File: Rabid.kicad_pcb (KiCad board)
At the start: 2 copper layers, 342.9 x 121.9 mm, 215 parts, among them J1 USB Header, SW1 Key, SW10 Key, SW100 Key, SW101 Key, SW102 Key, SW11 Key, SW12 Key, SW13 Key, SW14 Key, SW15 Key, SW16 Key, SW17 Key, SW18 Key, SW19 Key, SW2 Key, SW20 Key, SW21 Key, SW22 Key, SW23 Key, SW24 Key, SW25 Key, SW26 Key, SW27 Key, SW28 Key, SW29 Key, SW3 Key, SW30 Key, SW31 Key, SW32 Key, SW33 Key, SW34 Key, SW35 Key, SW36 Key, SW37 Key, SW38 Key, SW39 Key, SW4 Key, SW40 Key, SW41 Key, SW42 Key, SW43 Key, SW44 Key, SW45 Key, SW46 Key, SW47 Key, SW48 Key, SW49 Key, SW5 Key, SW50 Key, SW51 Key, SW52 Key, SW53 Key, SW54 Key, SW55 Key, SW56 Key, SW57 Key, SW58 Key, SW59 Key, SW6 Key, SW60 Key, SW61 Key, SW62 Key, SW63 Key, SW64 Key, SW65 Key, SW66 Key, SW67 Key, SW68 Key, SW69 Key, SW7 Key, SW70 Key, SW71 Key, SW72 Key, SW73 Key, SW74 Key, SW75 Key, SW76 Key, SW77 Key, SW78 Key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

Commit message: Everything in its approximate location.
TODO:
 - Still needs comparison to a real PCB to get measurements more accurate.
 - Needs mounting holes.
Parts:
- removed D100, D101, D24, D30, D36, D48, D54, D60, D7, D77, D82, D83, D88, D89, D94: 1N4148, Diode_THT:D_DO-35_SOD27_P7.62mm_Horizontal
- removed SW100, SW101, SW24, SW30, SW36, SW48, SW54, SW60, SW7, SW77, SW82, SW83, SW88, SW89, SW94: Key, Button_Switch_Keyboard:SW_Cherry_MX_1.00u_PCB
- SW12, SW18, SW6, SW66, SW72, SW78, SW84: footprint Button_Switch_Keyboard:SW_Cherry_MX_1.00u_PCB -> Button_Switch_Keyboard:SW_Cherry_MX_1.25u_PCB
- SW3, SW81: footprint Button_Switch_Keyboard:SW_Cherry_MX_1.00u_PCB -> Button_Switch_Keyboard:SW_Cherry_MX_1.50u_PCB
- SW4: footprint Button_Switch_Keyboard:SW_Cherry_MX_1.00u_PCB -> Button_Switch_Keyboard:SW_Cherry_MX_1.75u_PCB
- SW42: footprint Button_Switch_Keyboard:SW_Cherry_MX_1.00u_PCB -> Button_Switch_Keyboard:SW_Cherry_MX_6.25u_PCB
- SW5, SW76: footprint Button_Switch_Keyboard:SW_Cherry_MX_1.00u_PCB -> Button_Switch_Keyboard:SW_Cherry_MX_2.25u_PCB
- SW71: footprint Button_Switch_Keyboard:SW_Cherry_MX_1.00u_PCB -> Button_Switch_Keyboard:SW_Cherry_MX_2.75u_PCB
- SW80: footprint Button_Switch_Keyboard:SW_Cherry_MX_1.00u_PCB -> Button_Switch_Keyboard:SW_Cherry_MX_2.00u_PCB
- moved R2 420.4 mm to (335.5, 99.8)
- moved D91 413.8 mm to (348.0, 90.8), turned to 90 degrees
- moved D104 395.8 mm to (346.7, 99.6)
- moved D55 386.2 mm to (219.1, 90.8), turned to 90 degrees
- moved D99 384.1 mm to (367.7, 137.8), turned to 90 degrees
- moved D62 381.6 mm to (229.2, 118.7), turned to 90 degrees
- moved D87 366.9 mm to (328.9, 137.8), turned to 90 degrees
- moved D43 365.2 mm to (181.0, 90.8), turned to 90 degrees
- moved D2 359.4 mm to (51.3, 103.4), turned to 180 degrees
- moved R3 359.3 mm to (335.5, 103.4)
- moved D106 352.6 mm to (365.8, 99.8)
- moved D81 350.9 mm to (298.4, 137.8), turned to 90 degrees
- moved D1 347.3 mm to (57.4, 90.7), turned to 90 degrees
- moved D20 346.1 mm to (95.2, 118.7), turned to 90 degrees
- moved D49 346.0 mm to (200.0, 90.8), turned to 90 degrees
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
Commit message: Name the keys on F.Fab layer.
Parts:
- SW1: value Key -> Esc
- SW10: value Key -> A
- SW102: value Key -> →
- SW11: value Key -> Z
- SW12: value Key -> LMeta
- SW13: value Key -> F1
- SW14: value Key -> 2
- SW15: value Key -> W
- SW16: value Key -> S
- SW17: value Key -> X
- SW18: value Key -> LAlt
- SW19: value Key -> F2
- SW2: value Key -> ~
- SW20: value Key -> 3
- SW21: value Key -> E
- SW22: value Key -> D
- SW23: value Key -> C
- SW25: value Key -> F3
- SW26: value Key -> 4
- SW27: value Key -> R
- SW28: value Key -> F
- SW29: value Key -> V
- SW3: value Key -> Tab
- SW31: value Key -> F4
- SW32: value Key -> 5
- SW33: value Key -> T
- SW34: value Key -> G
- SW35: value Key -> B
- SW37: value Key -> F5
- SW38: value Key -> 6
- SW39: value Key -> Y
- SW4: value Key -> CapsLk
- SW40: value Key -> H
- SW41: value Key -> N
- SW42: value Key -> Space
- SW43: value Key -> F6
- SW44: value Key -> 7
- SW45: value Key -> U
- SW46: value Key -> J
- SW47: value Key -> M
- SW49: value Key -> F7
- SW5: value Key -> LShift
- SW50: value Key -> 8
- SW51: value Key -> I
- SW52: value Key -> K
- SW53: value Key -> ,
- SW55: value Key -> F8
- SW56: value Key -> 9
- SW57: value Key -> O
- SW58: value Key -> L
- SW59: value Key -> .
- SW6: value Key -> LCtrl
- SW61: value Key -> F9
- SW62: value Key -> 0
- SW63: value Key -> P
- SW64: value Key -> ;
- SW65: value Key -> /
- SW66: value Key -> AltGr
- SW67: value Key -> F10
- SW68: value Key -> -
- SW69: value Key -> [
- SW70: value Key -> "
- SW71: value Key -> RShift
- SW72: value Key -> RMeta
- SW73: value Key -> F11
- SW74: value Key -> =
- SW75: value Key -> ]
- SW76: value Key -> ↲
- SW78: value Key -> Fn
- SW79: value Key -> F12
- SW8: value Key -> 1
- SW80: value Key -> BkSpc
- SW81: value Key -> \
- SW84: value Key -> RCtrl
- SW85: value Key -> PrtSc
- SW86: value Key -> Ins
- SW87: value Key -> Del
- SW9: value Key -> Q
- SW90: value Key -> ←
- SW91: value Key -> ScrLk
- SW92: value Key -> Home
- SW93: value Key -> End
- SW95: value Key -> ↑
- SW96: value Key -> ↓
- SW97: value Key -> Pause
- SW98: value Key -> PgUp
- SW99: value Key -> PgDn

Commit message: Made measurements more precise.
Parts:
- J1: moved to B.Cu
- moved J1 57.4 mm to (295.7, 96.5), turned to 90 degrees
- moved SW1 0.25 mm to (50.2, 80.9)
- moved D105 0.13 mm to (356.2, 90.8)
- moved D107 0.13 mm to (255.9, 90.8)
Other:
- board size 342.9 x 121.9 mm -> 344.6 x 122 mm
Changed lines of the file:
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@@
       (effects (font (size 0.9 0.9) (thickness 0.12)))
     )
-    (fp_text user "0" (at -4.0372 -11.2 unlocked) (layer "F.SilkS")
+    (fp_text user "0" (at -11.303 -11.176 unlocked) (layer "F.SilkS")
       (effects (font (size 0.9 0.9) (thickness 0.12)))
     )
@@
     )
   )
-  (footprint "Connector_JST:JST_PH_S5B-PH-SM4-TB_1x05-1MP_P2.00mm_Horizontal" (layer "F.Cu")
-    (at 238.252 98.044 -90)
-    (descr "JST PH series connector, S5B-PH-SM4-TB (http://www.jst-mfg.com/product/pdf/eng/ePH.pdf), generated with kicad-footprint-generator")
-    (tags "connector JST PH top entry")
-    (property "Sheetfile" "Rabid.kicad_sch")
-    (property "Sheetname" "")
-    (attr smd)
-    (fp_text reference "J1" (at 0 -5.8 90) (layer "F.SilkS")
-      (effects (font (size 1 1) (thickness 0.15)))
-    )
-    (fp_text value "USB Header" (at 0 5.8 90) (layer "F.Fab")
-      (effects (font (size 1 1) (thickness 0.15)))
-    )
-    (fp_text user "${REFERENCE}" (at 0 1.5 90) (layer "F.Fab")
-      (effects (font (size 1 1) (thickness 0.15)))
-    )
-    (fp_line (start -5.34 4.51) (end 5.34 4.51) (layer "F.SilkS") (width 0.12))
-    (fp_line (start -6.04 -3.31) (end -6.04 -1.71) (layer "F.SilkS") (width 0.12))
-    (fp_line (start 7.06 0.94) (end 7.06 -3.31) (layer "F.SilkS") (width 0.12))
-    (fp_line (start 6.04 -3.31) (end 6.04 -1.71) (layer "F.SilkS") (width 0.12))
-    (fp_line (start -4.76 -1.71) (end -4.76 -4.6) (layer "F.SilkS") (width 0.12))
-    (fp_line (start -7.06 -3.31) (end -6.04 -3.31) (layer "F.SilkS") (width 0.12))
-    (fp_line (start 6.04 -1.71) (end 4.76 -1.71) (layer "F.SilkS") (width 0.12))
-    (fp_line (start 7.06 -3.31) (end 6.04 -3.31) (layer "F.SilkS") (width 0.12))
-    (fp_line (start -7.06 0.94) (end -7.06 -3.31) (layer "F.SilkS") (width 0.12))
-    (fp_line (start -6.04 -1.71) (end -4.76 -1.71) (layer "F.SilkS") (width 0.12))
-    (fp_line (start 7.6 5.1) (end 7.6 -5.1) (layer "F.CrtYd") (width 0.05))
-    (fp_line (start -7.6 5.1) (end 7.6 5.1) (layer "F.CrtYd") (width 0.05))
-    (fp_line (start -7.6 -5.1) (end -7.6 5.1) (layer "F.CrtYd") (width 0.05))
-    (fp_line (start 7.6 -5.1) (end -7.6 -5.1) (layer "F.CrtYd") (width 0.05))
-    (fp_line (start -6.95 -3.2) (end -6.15 -3.2) (layer "F.Fab") (width 0.1))
-    (fp_line (start 6.95 -3.2) (end 6.95 4.4) (layer "F.Fab") (width 0.1))
-    (fp_line (start -6.95 4.4) (end 6.95 4.4) (layer "F.Fab") (width 0.1))
-    (fp_line (start -4 -0.892893) (end -3.5 -1.6) (layer "F.Fab") (width 0.1))
-    (fp_line (start 6.15 -3.2) (end 6.95 -3.2) (layer "F.Fab") (width 0.1))
-    (fp_line (start -6.15 -3.2) (end -6.15 -1.6) (layer "F.Fab") (width 0.1))
-    (fp_line (start 6.15 -1.6) (end 6.15 -3.2) (layer "F.Fab") (width 0.1))
-    (fp_line (start -6.95 -3.2) (end -6.95 4.4) (layer "F.Fab") (width 0.1))
-    (fp_line (start -4.5 -1.6) (end -4 -0.892893) (layer "F.Fab") (width 0.1))
-    (fp_line (start -6.15 -1.6) (end 6.15 -1.6) (layer "F.Fab") (width 0.1))
-    (pad "1" smd roundrect (at -4 -2.85 270) (size 1 3.5) (layers "F.Cu" "F.Paste" "F.Mask") (roundrect_rratio 0.25)
-      (net 107 "Net-(J1-Pad1)") (pinfunction "Pin_1") (pintype "passive"))
-    (pad "2" smd roundrect (at -2 -2.85 270) (size 1 3.5) (layers "F.Cu" "F.Paste" "F.Mask") (roundrect_rratio 0.25)
-      (net 108 "Net-(J1-Pad2)") (pinfunction "Pin_2") (pintype "passive"))
-    (pad "3" smd roundrect (at 0 -2.85 270) (size 1 3.5) (layers "F.Cu" "F.Paste" "F.Mask") (roundrect_rratio 0.25)
-      (net 109 "Net-(J1-Pad3)") (pinfunction "Pin_3") (pintype "passive"))
-    (pad "4" smd roundrect (at 2 -2.85 270) (size 1 3.5) (layers "F.Cu" "F.Paste" "F.Mask") (roundrect_rratio 0.25)
-      (net 33 "GND") (pinfunction "Pin_4") (pintype "passive"))
-    (pad "5" smd roundrect (at 4 -2.85 270) (size 1 3.5) (layers "F.Cu" "F.Paste" "F.Mask") (roundrect_rratio 0.25)
-      (net 110 "unconnected-(J1-Pad5)") (pinfunction "Pin_5") (pintype "passive"))
-    (pad "MP" smd roundrect (at 6.35 2.9 270) (size 1.5 3.4) (layers "F.Cu" "F.Paste" "F.Mask") (roundrect_rratio 0.166667))
-    (pad "MP" smd roundrect (at -6.35 2.9 270) (size 1.5 3.4) (layers "F.Cu" "F.Paste" "F.Mask") (roundrect_rratio 0.166667))
-    (model "${KICAD6_3DMODEL_DIR}/Connector_JST.3dshapes/JST_PH_S5B-PH-SM4-TB_1x05-1MP_P2.00mm_Horizontal.wrl"
-      (offset (xyz 0 0 0))
-      (scale (xyz 1 1 1))
-      (rotate (xyz 0 0 0))
-    )
-  )
   (footprint "Button_Switch_Keyboard:SW_Cherry_MX_1.00u_PCB" (layer "F.Cu")
     (at 169.2402 165.7858)
@@
   )
   (footprint "Button_Switch_Keyboard:SW_Cherry_MX_1.00u_PCB" (layer "F.Cu")
-    (at 50.165 80.645)
+    (at 50.165 80.899)
     (descr "Cherry MX keyswitch, 1.00u, PCB mount, http://cherryamericas.com/wp-content/uploads/2014/12/mx_cat.pdf")
     (tags "Cherry MX keyswitch 1.00u PCB")
@@
   )
   (footprint "LED_THT:LED_D3.0mm" (layer "F.Cu")
-    (at 356.23 90.932)
+    (at 356.23 90.805)
     (descr "LED, diameter 3.0mm, 2 pins")
     (tags "LED diameter 3.0mm 2 pins")
@@
   )
   (footprint "LED_THT:LED_D3.0mm" (layer "F.Cu")
-    (at 255.9 90.932)
+    (at 255.9 90.805)
     (descr "LED, diameter 3.0mm, 2 pins")
     (tags "LED diameter 3.0mm 2 pins")
@@
     )
   )
-  (gr_rect (start 40.386 76.2) (end 383.286 198.12) (layer "Edge.Cuts") (width 0.1) (fill none))
+  (footprint "Connector_JST:JST_PH_S5B-PH-SM4-TB_1x05-1MP_P2.00mm_Horizontal" (layer "B.Cu")
+    (at 295.656 96.52 90)
+    (descr "JST PH series connector, S5B-PH-SM4-TB (http://www.jst-mfg.com/product/pdf/eng/ePH.pdf), generated with kicad-footprint-generator")
+    (tags "connector JST PH top entry")
+    (property "Sheetfile" "Rabid.kicad_sch")
+    (property "Sheetname" "")
+    (attr smd)
+    (fp_text reference "J1" (at 0 5.8 90) (layer "B.SilkS")
+      (effects (font (size 1 1) (thickness 0.15)) (justify mirror))
+    )
+    (fp_text value "USB Header" (at 0 -5.8 90) (layer "B.Fab")
+      (effects (font (size 1 1) (thickness 0.15)) (justify mirror))
+    )
+    (fp_text user "${REFERENCE}" (at 0 -1.5 90) (layer "B.Fab")
+      (effects (font (size 1 1) (thickness 0.15)) (justify mirror))
+    )
+    (fp_line (start -5.34 -4.51) (end 5.34 -4.51) (layer "B.SilkS") (width 0.12))
+    (fp_line (start -6.04 3.31) (end -6.04 1.71) (layer "B.SilkS") (width 0.12))
+    (fp_line (start 7.06 -0.94) (end 7.06 3.31) (layer "B.SilkS") (width 0.12))
+    (fp_line (start 6.04 3.31) (end 6.04 1.71) (layer "B.SilkS") (width 0.12))
+    (fp_line (start -4.76 1.71) (end -4.76 4.6) (layer "B.SilkS") (width 0.12))
+    (fp_line (start -7.06 3.31) (end -6.04 3.31) (layer "B.SilkS") (width 0.12))
+    (fp_line (start 6.04 1.71) (end 4.76 1.71) (layer "B.SilkS") (width 0.12))
+    (fp_line (start 7.06 3.31) (end 6.04 3.31) (layer "B.SilkS") (width 0.12))
+    (fp_line (start -7.06 -0.94) (end -7.06 3.31) (layer "B.SilkS") (width 0.12))
+    (fp_line (start -6.04 1.71) (end -4.76 1.71) (layer "B.SilkS") (width 0.12))
+    (fp_line (start 7.6 -5.1) (end 7.6 5.1) (layer "B.CrtYd") (width 0.05))
+    (fp_line (start -7.6 -5.1) (end 7.6 -5.1) (layer "B.CrtYd") (width 0.05))
+    (fp_line (start -7.6 5.1) (end -7.6 -5.1) (layer "B.CrtYd") (width 0.05))
+    (fp_line (start 7.6 5.1) (end -7.6 5.1) (layer "B.CrtYd") (width 0.05))
+    (fp_line (start -6.95 3.2) (end -6.15 3.2) (layer "B.Fab") (width 0.1))
+    (fp_line (start 6.95 3.2) (end 6.95 -4.4) (layer "B.Fab") (width 0.1))
+    (fp_line (start -6.95 -4.4) (end 6.95 -4.4) (layer "B.Fab") (width 0.1))
+    (fp_line (start -4 0.892893) (end -3.5 1.6) (layer "B.Fab") (width 0.1))
+    (fp_line (start 6.15 3.2) (end 6.95 3.2) (layer "B.Fab") (width 0.1))
+    (fp_line (start -6.15 3.2) (end -6.15 1.6) (layer "B.Fab") (width 0.1))
+    (fp_line (start 6.15 1.6) (end 6.15 3.2) (layer "B.Fab") (width 0.1))
+    (fp_line (start -6.95 3.2) (end -6.95 -4.4) (layer "B.Fab") (width 0.1))
+    (fp_line (start -4.5 1.6) (end -4 0.892893) (layer "B.Fab") (width 0.1))
+    (fp_line (start -6.15 1.6) (end 6.15 1.6) (layer "B.Fab") (width 0.1))
+    (pad "1" smd roundrect (at -4 2.85 90) (size 1 3.5) (layers "B.Cu" "B.Paste" "B.Mask") (roundrect_rratio 0.25)
+      (net 107 "Net-(J1-Pad1)") (pinfunction "Pin_1") (pintype "passive"))
+    (pad "2" smd roundrect (at -2 2.85 90) (size 1 3.5) (layers "B.Cu" "B.Paste" "B.Mask") (roundrect_rratio 0.25)
+      (net 108 "Net-(J1-Pad2)") (pinfunction "Pin_2") (pintype "passive"))
+    (pad "3" smd roundrect (at 0 2.85 90) (size 1 3.5) (layers "B.Cu" "B.Paste" "B.Mask") (roundrect_rratio 0.25)
+      (net 109 "Net-(J1-Pad3)") (pinfunction "Pin_3") (pintype "passive"))
+    (pad "4" smd roundrect (at 2 2.85 90) (size 1 3.5) (layers "B.Cu" "B.Paste" "B.Mask") (roundrect_rratio 0.25)
+      (net 33 "GND") (pinfunction "Pin_4") (pintype "passive"))
+    (pad "5" smd roundrect (at 4 2.85 90) (size 1 3.5) (layers "B.Cu" "B.Paste" "B.Mask") (roundrect_rratio 0.25)
+      (net 110 "unconnected-(J1-Pad5)") (pinfunction "Pin_5") (pintype "passive"))
+    (pad "MP" smd roundrect (at 6.35 -2.9 90) (size 1.5 3.4) (layers "B.Cu" "B.Paste" "B.Mask") (roundrect_rratio 0.166667))
+    (pad "MP" smd roundrect (at -6.35 -2.9 90) (size 1.5 3.4) (layers "B.Cu" "B.Paste" "B.Mask") (roundrect_rratio 0.166667))
+    (model "${KICAD6_3DMODEL_DIR}/Connector_JST.3dshapes/JST_PH_S5B-PH-SM4-TB_1x05-1MP_P2.00mm_Horizontal.wrl"
+      (offset (xyz 0 0 0))
+      (scale (xyz 1 1 1))
+      (rotate (xyz 0 0 0))
+    )
+  )
+  (gr_rect (start 39.624 76.962) (end 384.175 199.009) (layer "Edge.Cuts") (width 0.1) (fill none))
   (dimension (type aligned) (layer "Eco2.User")
     (pts (xy 323.85 75.565) (xy 328.93 75.565))

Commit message: Add mounting holes.
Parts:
- added H1: MountingHole.35in, MountingHole:MountingHole_4.3mm_M4, F.Cu at (95.2, 99.8)
- added H2: MountingHole.35in, MountingHole:MountingHole_4.3mm_M4, F.Cu at (180.3, 99.8)
- added H3: MountingHole.35in, MountingHole:MountingHole_4.3mm_M4, F.Cu at (212.9, 99.8)
- added H4: MountingHole.35in, MountingHole:MountingHole_4.3mm_M4, F.Cu at (326.4, 99.6)
- added H5: MountingHole.35in, MountingHole:MountingHole_4.3mm_M4, F.Cu at (69.1, 150.9)
- added H6: MountingHole.25in, MountingHole:MountingHole_4.3mm_M4, F.Cu at (75.4, 161.3)
- added H7: MountingHole.35in, MountingHole:MountingHole_4.3mm_M4, F.Cu at (326.1, 185.7)
- moved D90 14.8 mm to (342.4, 180.6), turned to 180 degrees
- moved D96 8.76 mm to (348.0, 194.8), turned to 90 degrees
- moved D10 7.96 mm to (63.2, 155.7)
- moved D102 7.50 mm to (367.3, 194.8), turned to 90 degrees

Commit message: LED tracks routed.
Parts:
- moved R1 63.0 mm to (352.6, 157.0)
- moved R2 56.2 mm to (352.6, 153.4)
- moved R3 49.5 mm to (352.6, 149.9)
- moved D76 0.77 mm to (285.0, 157.0)
- moved D3 0.76 mm to (43.2, 137.7)
- moved D71 0.51 mm to (276.2, 175.8)
- moved D46 0.51 mm to (186.1, 157.0)
- moved D10 0.25 mm to (63.2, 156.0)
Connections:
- R1 pad 2: Net-(D103-Pad2) -> Net-(D105-Pad2)
- R2 pad 1: Net-(R2-Pad1) -> Net-(U1-Pad29)
- R2 pad 2: Net-(D105-Pad2) -> Net-(D107-Pad2)
- R3 pad 1: Net-(R3-Pad1) -> Net-(U1-Pad30)
- R3 pad 2: Net-(D107-Pad2) -> Net-(D103-Pad2)
- U1 pad 24: Net-(R1-Pad1) -> unconnected-(U1-Pad24)
- U1 pad 25: Net-(R2-Pad1) -> unconnected-(U1-Pad25)
- U1 pad 26: Net-(R3-Pad1) -> unconnected-(U1-Pad26)
- U1 pad 28: unconnected-(U1-Pad28) -> Net-(R1-Pad1)
- U1 pad 29: unconnected-(U1-Pad29) -> Net-(U1-Pad29)
- U1 pad 30: unconnected-(U1-Pad30) -> Net-(U1-Pad30)
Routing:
- net GND: track 0.00 -> 617.8 mm, vias 0 -> 2
- net Net-(D103-Pad2): track 0.00 -> 446.3 mm
- net Row0: track 0.00 -> 337.4 mm
- net Row4: track 0.00 -> 329.2 mm
- net Row5: track 0.00 -> 329.0 mm
- net Row3: track 0.00 -> 324.2 mm
- net Row2: track 0.00 -> 249.5 mm
- net Row1: track 0.00 -> 238.6 mm
- net Net-(D107-Pad2): track 0.00 -> 163.8 mm
- net ColL: track 0.00 -> 138.5 mm
- net ColK: track 0.00 -> 134.7 mm
- net ColG: track 0.00 -> 127.6 mm
- net ColA: track 0.00 -> 126.0 mm
- net ColM: track 0.00 -> 123.2 mm
- net ColC: track 0.00 -> 121.2 mm
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
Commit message: Tidy up the USB connector nets.
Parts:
- SW2: value ~ -> Tilde
- moved D10 0.51 mm to (62.7, 156.0)
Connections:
- net Net-(J1-Pad1) renamed +5V
- net Net-(J1-Pad2) renamed /USB_D-
- net Net-(J1-Pad3) renamed /USB_D+
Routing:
- net GND: track 617.8 -> 615.9 mm
- net +5V: track 74.6 -> 73.4 mm
- net /USB_D+: track 76.1 -> 77.2 mm
- net Net-(D10-Pad2): track 16.4 -> 17.2 mm
- net ColB: track 99.7 -> 100.3 mm
- net /USB_D-: track 75.9 -> 76.4 mm

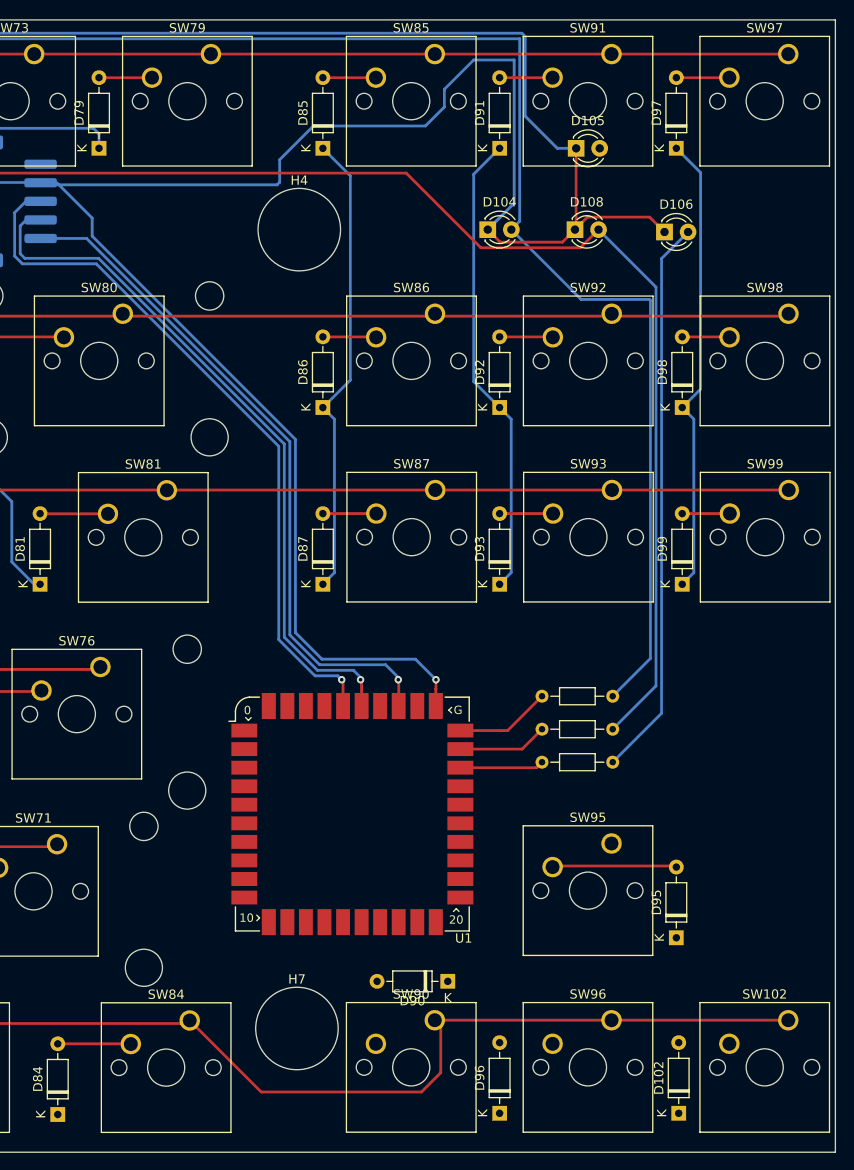
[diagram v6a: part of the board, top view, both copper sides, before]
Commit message: Routed arrows keys and rows.
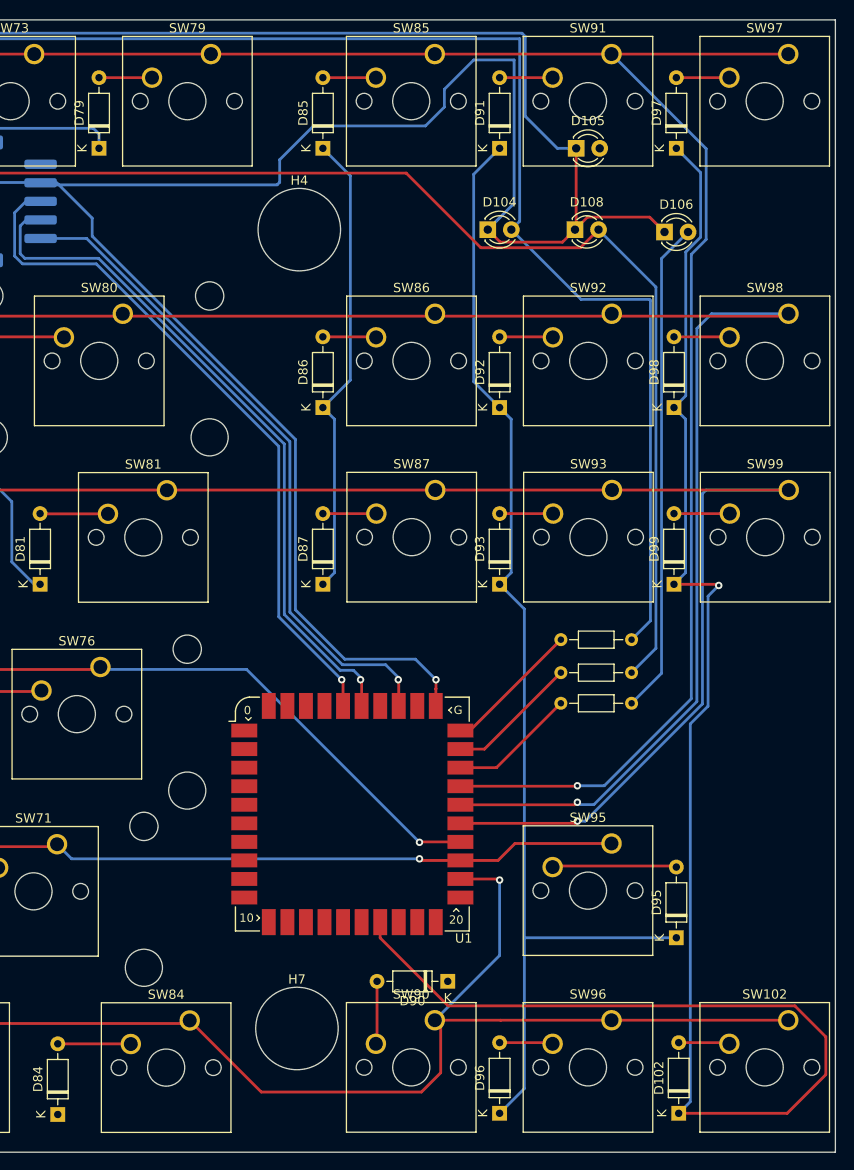
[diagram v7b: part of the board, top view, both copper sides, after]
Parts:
- moved R1 6.67 mm to (354.6, 150.6)
- moved R2 6.43 mm to (354.6, 147.3)
- moved R3 6.43 mm to (354.6, 143.8)
- moved D98 0.89 mm to (366.8, 118.7)
- moved D99 0.89 mm to (366.8, 137.8)
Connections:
- U1 pad 1: Row5 -> ColA
- U1 pad 10: ColD -> ColJ
- U1 pad 11: ColE -> ColK
- U1 pad 12: ColF -> ColL
- U1 pad 13: ColG -> ColM
- U1 pad 14: ColH -> ColN
- U1 pad 15: ColI -> ColO
- U1 pad 16: ColJ -> ColP
- U1 pad 17: ColK -> ColQ
- U1 pad 18: ColL -> unconnected-(U1-Pad18)
- U1 pad 19: ColM -> unconnected-(U1-Pad19)
- U1 pad 2: Row4 -> ColB
- U1 pad 20: ColN -> unconnected-(U1-Pad20)
- U1 pad 21: ColO -> unconnected-(U1-Pad21)
- U1 pad 22: ColP -> Row0
- U1 pad 23: ColQ -> Row1
- U1 pad 24: unconnected-(U1-Pad24) -> Row2
- U1 pad 25: unconnected-(U1-Pad25) -> Row3
- U1 pad 26: unconnected-(U1-Pad26) -> Row4
- U1 pad 27: unconnected-(U1-Pad27) -> Row5
- U1 pad 3: Row3 -> ColC
- U1 pad 4: Row2 -> ColD
- U1 pad 5: Row1 -> ColE
- U1 pad 6: Row0 -> ColF
- U1 pad 7: ColA -> ColG
- U1 pad 8: ColB -> ColH
- U1 pad 9: ColC -> ColI
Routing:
- net ColQ: track 49.9 -> 189.7 mm, vias 0 -> 1
- net Row5: track 329.0 -> 432.2 mm, vias 0 -> 1
- net Row4: track 329.2 -> 410.3 mm, vias 0 -> 1
- net ColP: track 50.3 -> 126.0 mm
- net Row3: track 324.2 -> 387.8 mm, vias 0 -> 1
- net Row1: track 238.6 -> 299.9 mm, vias 0 -> 1
- net Row2: track 249.5 -> 296.1 mm, vias 0 -> 1
- net Row0: track 337.4 -> 359.7 mm, vias 0 -> 1
- net Net-(D105-Pad2): track 61.0 -> 53.8 mm
- net Net-(D103-Pad2): track 446.3 -> 439.3 mm
- net Net-(D107-Pad2): track 163.8 -> 156.9 mm
- net Net-(D90-Pad2): track 0.00 -> 6.78 mm
- net Net-(D96-Pad2): track 0.00 -> 5.77 mm
- net Net-(D102-Pad2): track 0.00 -> 5.51 mm
- net Net-(R1-Pad1): track 9.04 -> 13.7 mm
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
